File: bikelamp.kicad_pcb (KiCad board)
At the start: 2 copper layers, 56.5 x 60.1 mm, 83 parts, among them J1 Conn_ARM_SWD_TagConnect_TC203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, J2 Conn_01x04_Pin, Q1 Q_PMOS_GSD, Q2 BSS138, Q3 RBFET, Q4 HIGH, Q5 LOW, Q6 ACFET, Q7 BSS138, Q8 YJQ3400A-YAN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

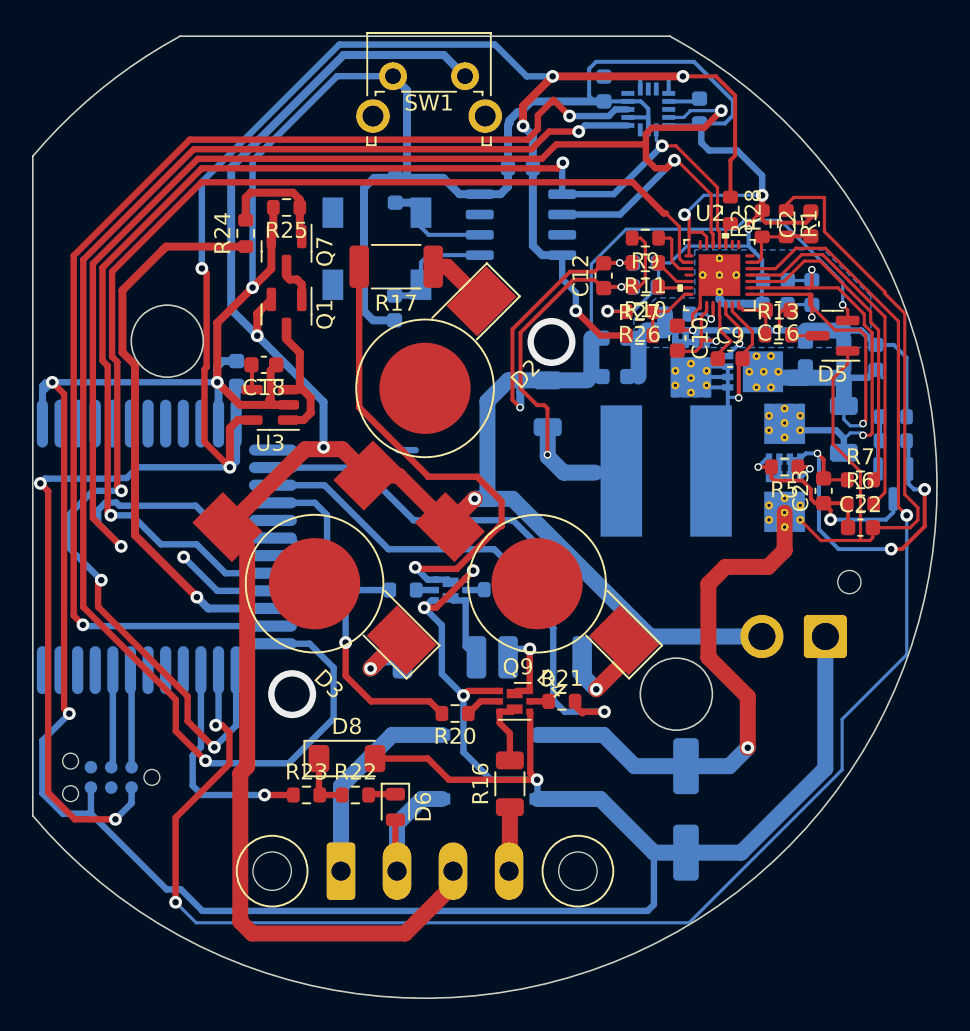
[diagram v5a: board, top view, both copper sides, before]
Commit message: - Get rid from <0.3 mm drills - Fine tune GND fill
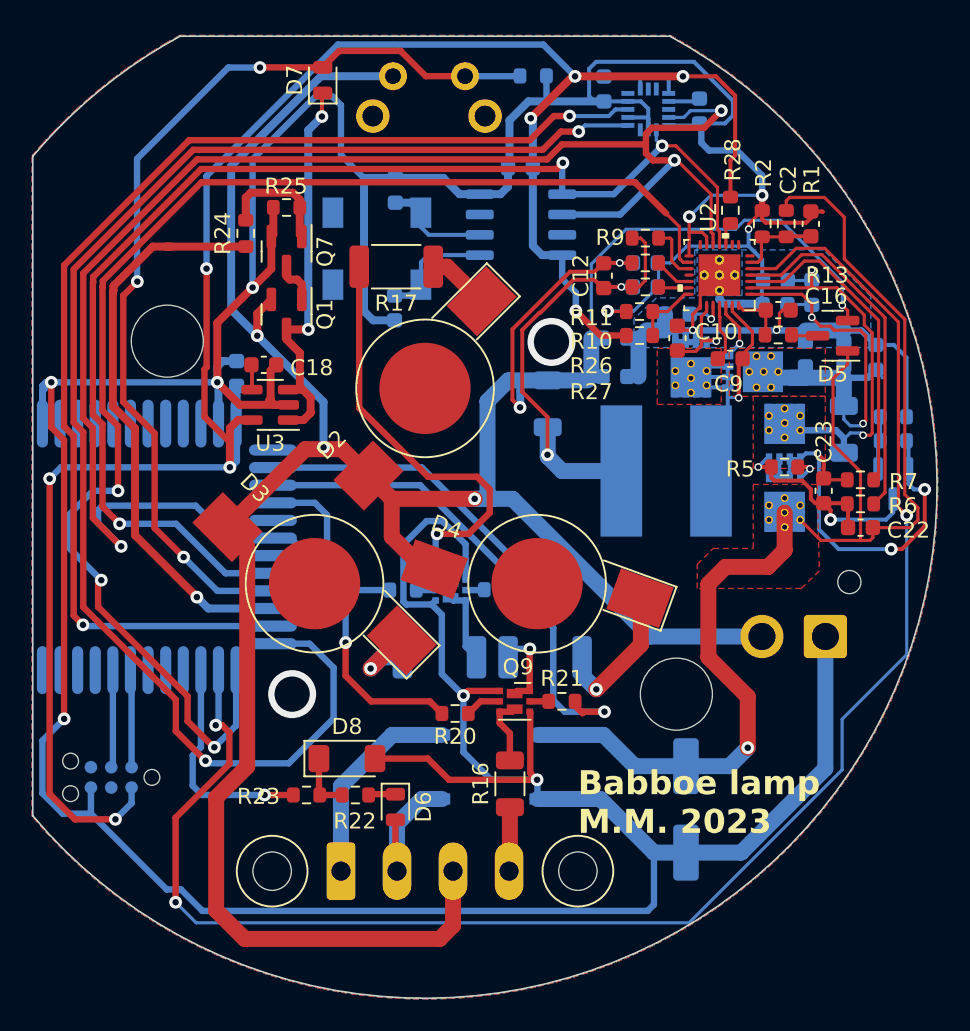
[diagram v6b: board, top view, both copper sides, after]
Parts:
- added D7: D_Schottky, Diode_SMD:D_MicroMELF, F.Cu at (3.61, 2.75)
- added R29: 10K, Resistor_SMD:R_0603_1608Metric, B.Cu at (16.8, 2.48)
- added REF**: MountingHole_4.5mm, MountingHole:MountingHole_4.5mm, F.Cu at (-6.10, 19.1)
- added REF**: MountingHole_4.5mm, MountingHole:MountingHole_4.5mm, F.Cu at (25.7, 41.1)
- R25: value 47 -> 10K
- SW1: moved to B.Cu
- U2: value BQ24780SRUYR -> RUY0028A
- moved SW1 4.50 mm to (12.5, 2.50), turned to 180 degrees
- turned D4 to 160 degrees
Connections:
- SW1 pad 1: GND -> PWR_BTN_PRESSED
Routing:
- net PWR_BTN_PRESSED: track 6.45 -> 60.7 mm, vias 1 -> 3
- net Net-(D7-K): track 8.30 -> 24.8 mm, vias 0 -> 2
- net GND: track 307.7 -> 313.3 mm, vias 12 -> 10
- net Net-(D4-K): track 6.15 -> 9.78 mm
- net Net-(Q8A-D): track 30.8 -> 28.3 mm
- net VBAT: track 168.1 -> 170.5 mm
- net /BQ24780/VIN_I_MEASURED: track 30.3 -> 28.8 mm
- net LED_PWM_2: track 34.5 -> 33.1 mm
- net KEEP_POWER: track 35.0 -> 36.3 mm
- net /BQ24780/SR_R_P: track 27.5 -> 28.7 mm
- net (no net): track 1.09 -> 0.00 mm
- net MMA8452_INT1: track 74.9 -> 74.1 mm
- net +3V3: track 141.1 -> 140.5 mm
- added copper zone on F.Cu, net /BQ24780/PHASE
- added copper zone on F.Cu, net /BQ24780/VIN_I_MEASURED
- added copper zone on F.Cu, net /BQ24780/VIN_REVPROT
- added copper zone on B.Cu, net GND
- added copper zone on F.Cu, net GND
- added copper zone on F.Cu, net VDD
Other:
- outline, holes or cut-outs redrawn
- board text added: "Babboe lamp M.M. 2023"
